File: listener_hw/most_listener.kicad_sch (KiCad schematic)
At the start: 74 parts, among them J1 1-1394640-1, J2 ANALYSER, J3 I2S, J4 VBAT_IN, M1 Tang Nano 20K, M2 ESP32-DevKitC-VIE, U1 74LVC1G34, U10 TPS2553DBVR, U11 74LVC1G123, U2 74LVC1G157, U3 74LVC1G125, U4 74LVC1G123, U5 TPS7B8133DRV, U6 LMR33630ADDA, U7 Si514, U8 LP5907MFX-3.3, U9 74LVC1G79

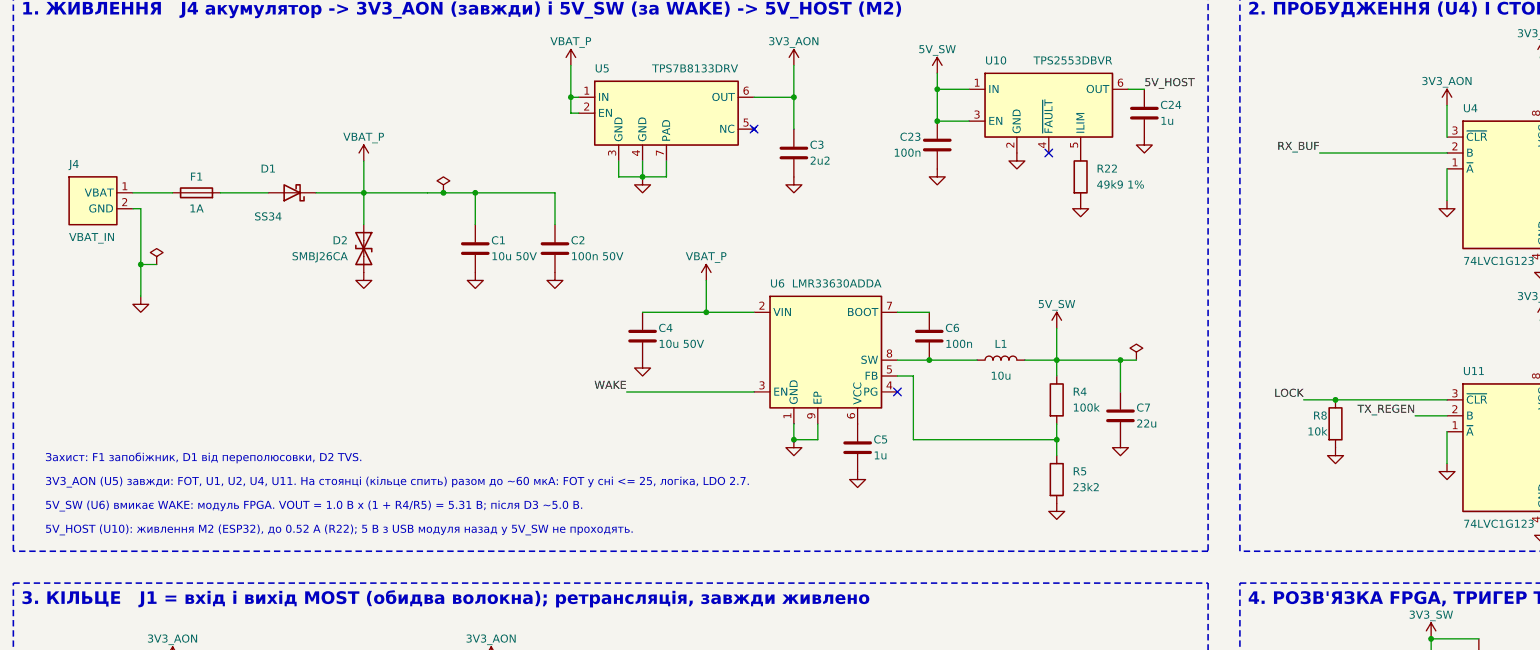
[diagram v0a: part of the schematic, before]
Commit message: Board: about 1 A for the host module's supply, not 0.52 A
U10 (TPS2553) limited 5V_HOST to 0.52 A typ (0.475-0.565 A, R22 49.9k).
Espressif asks for a 500 mA supply for the ESP32 module and its radio
draws it in peaks: a brown-out reset waiting to happen, with 1 uF behind
the switch. R22 24.9k (about 1 A; the limit scales with 1/R from the
table's 0.52 A at 49.9k), C24 10 uF. The sheet and its PDF regenerated;
ERC 0/0.

Co-Authored-By: Claude Fable 5.1 <noreply@anthropic.com>
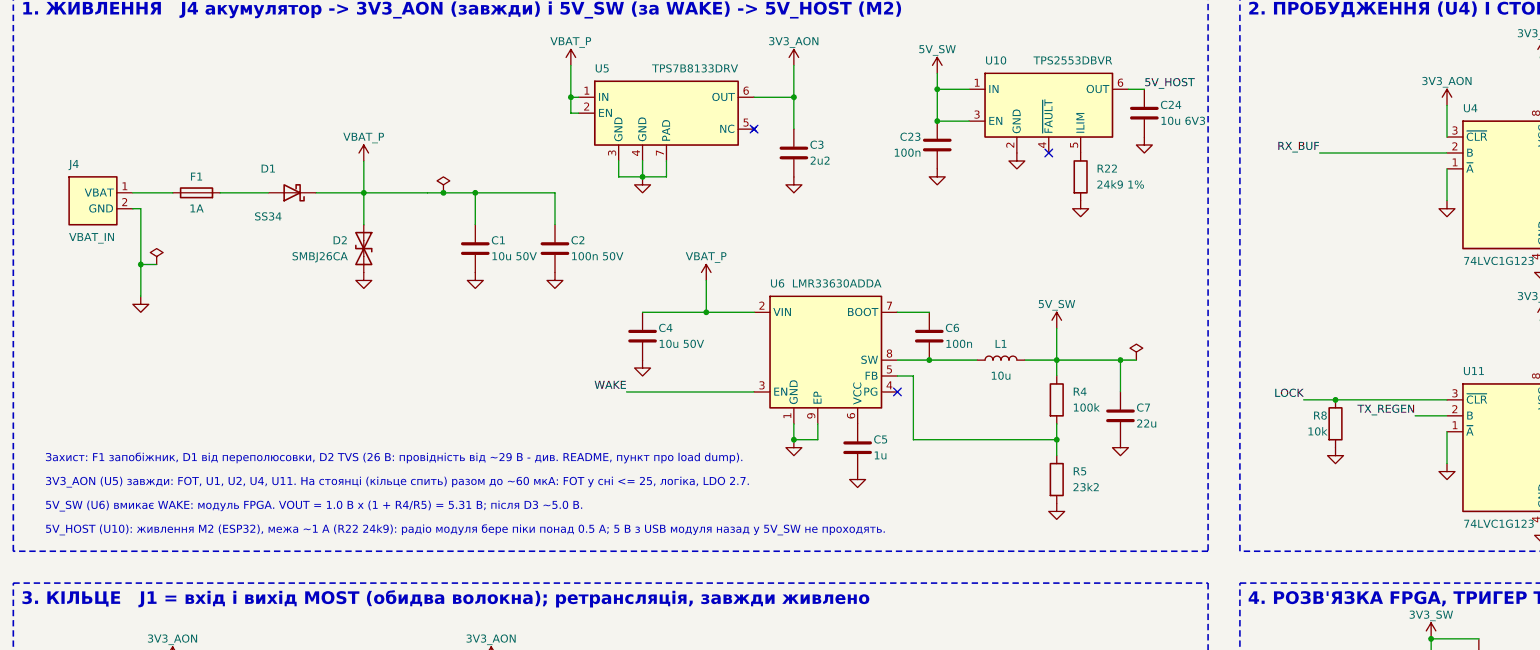
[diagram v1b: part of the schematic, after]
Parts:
- C24: value 1u -> 10u 6V3; footprint Capacitor_SMD:C_0603_1608Metric -> Capacitor_SMD:C_0805_2012Metric
- R22: value 49k9 1% -> 24k9 1%
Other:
- note added: "5V_HOST (U10): живлення M2 (ESP32), межа ~1 А (R22 24k9): радіо модуля бере піки понад 0.5 А; 5 В з USB модуля назад у 5V_SW не проходять."
- note added: "Захист: F1 запобіжник, D1 від переполюсовки, D2 TVS (26 В: провідність від ~29 В - див. README, пункт про load dump)."
- note removed: "5V_HOST (U10): живлення M2 (ESP32), до 0.52 А (R22); 5 В з USB модуля назад у 5V_SW не проходять."
- note removed: "Захист: F1 запобіжник, D1 від переполюсовки, D2 TVS."
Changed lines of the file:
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@@
   (pin "1")
   (instances (project "most_listener" (path "/1dba4ab3-cb1b-59ba-ab72-d256b8063c7a" (reference "#PWR007") (unit 1)))))
-(text "Захист: F1 запобіжник, D1 від переполюсовки, D2 TVS." (exclude_from_sim no) (at 17.78 87.63 0) (effects (font (size 1.27 1.27)) (justify left bottom)))
+(text "Захист: F1 запобіжник, D1 від переполюсовки, D2 TVS (26 В: провідність від ~29 В - див. README, пункт про load dump)." (exclude_from_sim no) (at 17.78 87.63 0) (effects (font (size 1.27 1.27)) (justify left bottom)))
 (text "3V3_AON (U5) завжди: FOT, U1, U2, U4, U11. На стоянці (кільце спить) разом до ~60 мкА: FOT у сні <= 25, логіка, LDO 2.7." (exclude_from_sim no) (at 17.78 91.44 0) (effects (font (size 1.27 1.27)) (justify left bottom)))
 (text "5V_SW (U6) вмикає WAKE: модуль FPGA. VOUT = 1.0 В x (1 + R4/R5) = 5.31 В; після D3 ~5.0 В." (exclude_from_sim no) (at 17.78 95.25 0) (effects (font (size 1.27 1.27)) (justify left bottom)))
-(text "5V_HOST (U10): живлення M2 (ESP32), до 0.52 А (R22); 5 В з USB модуля назад у 5V_SW не проходять." (exclude_from_sim no) (at 17.78 99.06 0) (effects (font (size 1.27 1.27)) (justify left bottom)))
+(text "5V_HOST (U10): живлення M2 (ESP32), межа ~1 А (R22 24k9): радіо модуля бере піки понад 0.5 А; 5 В з USB модуля назад у 5V_SW не проходять." (exclude_from_sim no) (at 17.78 99.06 0) (effects (font (size 1.27 1.27)) (justify left bottom)))
 (symbol (lib_id "most_listener:TPS7B8133DRV") (at 116.84 31.75 0) (unit 1) (exclude_from_sim no) (in_bom yes) (on_board yes) (dnp no)
   (property "Reference" "U5" (at 105.41 25.4 0) (effects (font (size 1.27 1.27)) (justify left bottom)))
@@
 (symbol (lib_id "Device:R") (at 182.88 41.91 0) (unit 1) (exclude_from_sim no) (in_bom yes) (on_board yes) (dnp no)
   (property "Reference" "R22" (at 185.42 40.64 0) (effects (font (size 1.27 1.27)) (justify left)))
-  (property "Value" "49k9 1%" (at 185.42 43.18 0) (effects (font (size 1.27 1.27)) (justify left)))
+  (property "Value" "24k9 1%" (at 185.42 43.18 0) (effects (font (size 1.27 1.27)) (justify left)))
   (property "Footprint" "Resistor_SMD:R_0603_1608Metric" (at 182.88 41.91 0) (effects (font (size 1.27 1.27)) (hide yes)))
   (property "Datasheet" "" (at 182.88 41.91 0) (effects (font (size 1.27 1.27)) (hide yes)))
@@
 (symbol (lib_id "Device:C") (at 193.04 31.75 0) (unit 1) (exclude_from_sim no) (in_bom yes) (on_board yes) (dnp no)
   (property "Reference" "C24" (at 195.58 30.48 0) (effects (font (size 1.27 1.27)) (justify left)))
-  (property "Value" "1u" (at 195.58 33.02 0) (effects (font (size 1.27 1.27)) (justify left)))
-  (property "Footprint" "Capacitor_SMD:C_0603_1608Metric" (at 193.04 31.75 0) (effects (font (size 1.27 1.27)) (hide yes)))
+  (property "Value" "10u 6V3" (at 195.58 33.02 0) (effects (font (size 1.27 1.27)) (justify left)))
+  (property "Footprint" "Capacitor_SMD:C_0805_2012Metric" (at 193.04 31.75 0) (effects (font (size 1.27 1.27)) (hide yes)))
   (property "Datasheet" "" (at 193.04 31.75 0) (effects (font (size 1.27 1.27)) (hide yes)))
   (pin "1") (pin "2")

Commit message: Board: block 9, TOSLINK in through DIR9001 and SRC4192, S/PDIF out on TOSLINK and coax
J5 (PLR135/T10) -> R25 -> U12 DIR9001 in hardware mode: PLL clock recovery
from the signal, 24-bit I2S out (FMT = HH), CKSEL = L, XTI to ground (no
crystal; the frequency calculator is not used), the loop filter of Table 6.
U13 SRC4192 with both ports slave (MODE = 000): the receiver's I2S on the
receiver's clock in (IFMT = 001), I2S 24 bit on the FPGA's BCLK/LRCK out
(OFMT = 01, OWL = 00) -> I2S_DIN2_F, pin 54. X1 24.576 MHz is the rate
estimator's reference (RCKI), asynchronous to both ports. One RC gives
both chips their reset 10 ms after 3V3_SW, when X1 already runs (the
SRC4192 has no power-on reset). U12's ERROR goes to M2 IO32 (OPT_ERR): 1 =
no lock or a parity error, so the host does not inject.

S/PDIF out: SPDIF_F (FPGA pin 31) -> R28 -> J6 (PLT133/T10W), and R26/R27
(0.5 V into 75 ohm from 75 ohm) + C29 -> J7, an RCA jack. Every pinout from
the data sheets (TI SLES198A, SBFS022C; Everlight PLR135, PLT133) or the
KiCad library (ASE oscillator, coaxial connector). The sheet is A2 now;
ERC: 0 violations; the PDF regenerated.

Co-Authored-By: Claude Fable 5.1 <noreply@anthropic.com>
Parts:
- added C27: 68n, Capacitor_SMD:C_0603_1608Metric, symbol Device:C
- added C28: 4n7, Capacitor_SMD:C_0603_1608Metric, symbol Device:C
- added C29, C30, C31, C32, C34, C36, C38, C39: 100n, Capacitor_SMD:C_0603_1608Metric, symbol Device:C
- added C33, C35, C37: 10u, Capacitor_SMD:C_0805_2012Metric, symbol Device:C
- added C40: 1u, Capacitor_SMD:C_0603_1608Metric, symbol Device:C
- added FB3: 600R, Inductor_SMD:L_0603_1608Metric, symbol Device:FerriteBead
- added J5: PLR135/T10, symbol most_listener:PLR135
- added J6: PLT133/T10W, symbol most_listener:PLT133
- added J7: RCA 75R, symbol Connector:Conn_Coaxial
- added R24: 680, Resistor_SMD:R_0603_1608Metric, symbol Device:R
- added R25: 100, Resistor_SMD:R_0603_1608Metric, symbol Device:R
- added R26: 240, Resistor_SMD:R_0603_1608Metric, symbol Device:R
- added R27: 110, Resistor_SMD:R_0603_1608Metric, symbol Device:R
- added R28, R29: 33, Resistor_SMD:R_0603_1608Metric, symbol Device:R
- added R30: 10k, Resistor_SMD:R_0603_1608Metric, symbol Device:R
- added U12: DIR9001, Package_SO:TSSOP-28_4.4x9.7mm_P0.65mm, symbol most_listener:DIR9001
- added U13: SRC4192, Package_SO:SSOP-28_5.3x10.2mm_P0.65mm, symbol most_listener:SRC4192
- added X1: 24.576MHz, Oscillator:Oscillator_SMD_Abracon_ASE-4Pin_3.2x2.5mm, symbol Oscillator:ASE-xxxMHz
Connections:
- net 3V3_SW: now also C31.1, C32.1, C33.1, C34.1, C35.1, C36.1, C37.1, C38.1, C39.1, FB3.2, J6.2 (VCC), R30.1, U12.24 (VCC), U12.25 (FMT0), U12.26 (FMT1), U12.5 (VDD), U13.10 (IFMT0), U13.19 (OFMT0), U13.22 (VDD), U13.7 (VIO), X1.1 (EN), X1.4 (Vdd)
- net GND: now also C27.2, C28.2, C30.2, C31.2, C32.2, C33.2, C34.2, C35.2, C36.2, C37.2, C38.2, C39.2, C40.2, J5.2 (GND), J6.3 (GND), J7.2 (Ext), R27.2, U12.13 (PSCK0), U12.14 (PSCK1), U12.19 (RSV), U12.23 (AGND), U12.28 (CKSEL), U12.6 (DGND), U12.8 (XTI), U13.1 (LGRP), U13.11 (IFMT1), U13.12 (IFMT2), U13.14 (MUTE), U13.16 (OWL1), U13.17 (OWL0), U13.18 (OFMT1), U13.20 (TDMI), U13.21 (DGND), U13.26 (MODE0), U13.27 (MODE1), U13.28 (MODE2), U13.8 (DGND), U13.9 (BYPAS), X1.2 (GND)
- net I2S_BCLK_F: now also U13.25 (BCKO)
- net I2S_LRCK_F: now also U13.24 (LRCKO)
- net SPDIF_F: now reaches M1.14 (31 LCD_B3)
- net SPDIF_F: now also R26.1, R28.1
- net I2S_DIN2_F: now reaches M1.28 (54 I2S_DIN)
- net I2S_DIN2_F: now also R29.2
- net OPT_ERR: now reaches M2.7 (IO32)
- net OPT_ERR: now also U12.27 (ERROR)
- new net: J6.1 (VIN), R28.2
- new net: C29.1, R26.2, R27.1
- new net: C29.2, J7.1 (In)
- new net: U13.2 (RCKI), X1.3 (OUT)
- new net: R29.1, U13.23 (SDOUT)
- new net: U12.12 (DOUT), U13.4 (SDIN)
- new net: U12.11 (BCKO), U13.5 (BCKI)
- new net: U12.10 (LRCKO), U13.6 (LRCKI)
- new net: C30.1, FB3.1, J5.3 (VCC)
- new net: C27.1, R24.1
- new net: C28.1, R24.2, U12.22 (FILT)
- new net: J5.1 (VOUT), R25.1
- new net: R25.2, U12.20 (RXIN)
- new net RST_AIN: C40.1, R30.2, U12.21 (RST), U13.13 (RST)
- no-connect marks 52 -> 63
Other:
- note added: "5V_SW (U6) вмикає WAKE: модуль FPGA, з його 3V3 (3V3_SW) - блок 9 (~0.1 А). VOUT = 1.0 В x (1 + R4/R5) = 5.31 В; після D3 ~5.0 В."
- note added: "9. ЦИФРОВЕ АУДІО J5 TOSLINK IN -> U12 DIR9001 -> U13 SRC4192 -> I2S_DIN2_F; SPDIF_F -> J6 TOSLINK OUT і J7 коаксіал"
- note added: "C31 J6; C32/C33 U12 VDD; C34/C35 U12 VCC;"
- note added: "C36/C37 U13 VDD; C38 U13 VIO; C39 X1: біля виводів."
- note added: "I2S slave: IO34/35 <- BCLK/LRCK, IO27 -> DIN; IO32 <- OPT_ERR."
- note added: "J3: I2S, BCLK 64 Fs, слоти 32 біт, 24 біт з регулюваннями ГУ; те саме S/PDIF - J6, J7 (блок 9)."
- note added: "J5 TOSLINK IN -> R25 -> U12 DIR9001: PLL відновлює такт із сигналу, вихід I2S 24 біт (FMT1 FMT0 = HH), CKSEL = L. XTI на землю: кварц не потрібен."
- note added: "OPT_ERR (U12 ERROR) -> M2 IO32: 1 = TOSLINK без сигналу або помилка парності; хост тоді не інжектує. Джерело для інжекції: команда 02, біт M[2]."
- note added: "S/PDIF OUT: SPDIF_F (FPGA 31) -> R28 -> J6 PLT133; R26/R27: 0.5 В на 75 Ом, вихідний опір 75 Ом; C29 без постійної -> J7 RCA. Той самий потік, що й на J3."
- note added: "U13 SRC4192: обидва порти slave (MODE = 000); вхід I2S 24 біт (IFMT = 001) від U12; вихід I2S 24 біт (OFMT = 01, OWL = 00) на тактах FPGA -> I2S_DIN2_F."
- note added: "X1 24.576 МГц: опорний такт оцінювача швидкості SRC4192 (RCKI), асинхронний до обох портів. RST_AIN: R30/C40 = 10 мс, коли X1 уже іде (SRC4192 без POR)."
- note added: "Кільце і Si514 - лише на виводах LCD (порожній роз'єм); S/PDIF на 31 (LCD_B3). HSPI, TF (80, 85), 54 (I2S_DIN вбудованого ЦАП): UART, MCLK, I2S, SD1, DIN2."
- note removed: "5V_SW (U6) вмикає WAKE: модуль FPGA. VOUT = 1.0 В x (1 + R4/R5) = 5.31 В; після D3 ~5.0 В."
- note removed: "I2S slave: IO34/35 <- BCLK/LRCK, IO27 -> DIN."
- note removed: "J3: I2S, BCLK 64 Fs, слоти 32 біт, 24 біт з регулюваннями ГУ."
- note removed: "Кільце і Si514 - лише на виводах LCD (порожній роз'єм). На HSPI і TF (80, 85) - лише UART, MCLK, I2S, SD1."

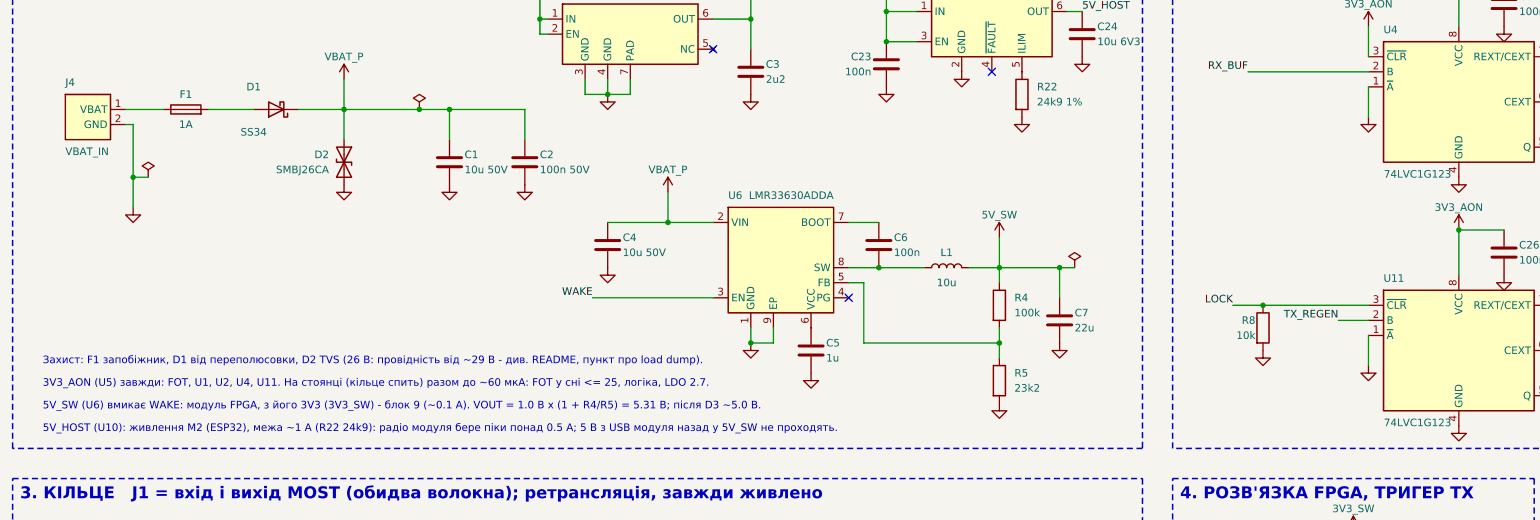
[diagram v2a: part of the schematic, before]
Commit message: Board: the battery input for ISO 16750-2 test B and ISO 7637-2 pulses - LMR38020, SMBJ36A before D1, a slow fuse
The SMBJ26CA behind the reverse diode conducted from 28.9 V: a suppressed
load dump (35 V, up to 400 ms, 0.5..4 ohm) that the buck itself survives
would have burnt it and blown F1, and a negative pulse 1 (-150 V, 10 ohm)
reached D1's 40 V reverse rating before any TVS clamped it. A TVS silent at
35 V clamps the fast pulses at 42..53 V, above the LMR33630's 38 V absolute
maximum, so the buck had to change too.

Now: U6 LMR38020F (4.2..80 V in, 85 V absolute maximum, 2 A, 400 kHz from
R31 = 64.9 k per Table 8-1, forced PWM so the frequency never falls into the
audio band; L1 15 uH and C7 47 uF per Table 9-1, CIN 4.7 uF + 100 nF at
100 V per 9.2.2.6; PG open, RT/SYNC never floats). D2 SMBJ36A,
unidirectional, between F1 and D1: silent at 35 V, clamps pulse 2a around
50 V, shunts negative pulses through its forward diode so D1 sees the
battery plus a volt. F1 2 A slow-blow: pulse 1 drives up to 15 A through the
TVS for 2 ms. C1, C2 rated 100 V for the clamped transients. Pins from TI
SNVSC40E Table 6-1 (the DDA pinout differs from the LMR33630's). Not
covered: the unsuppressed load dump (test A) - a 6.6 kW TVS's job. ERC 0
violations, PDF regenerated, README's open decision closed.

Co-Authored-By: Claude Fable 5.1 <noreply@anthropic.com>
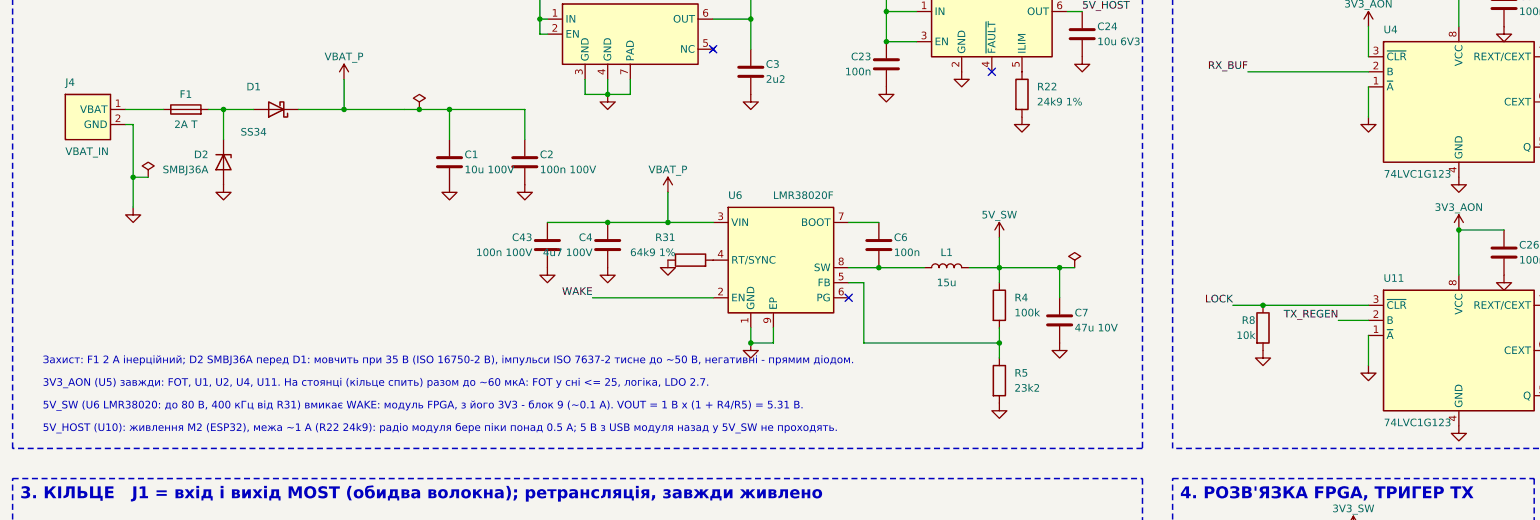
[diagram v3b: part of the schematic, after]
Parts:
- removed C5: 1u, Capacitor_SMD:C_0603_1608Metric, symbol Device:C
- added C43: 100n 100V, Capacitor_SMD:C_0603_1608Metric, symbol Device:C
- added R31: 64k9 1%, Resistor_SMD:R_0603_1608Metric, symbol Device:R
- C1: value 10u 50V -> 10u 100V
- C2: value 100n 50V -> 100n 100V
- C4: value 10u 50V -> 4u7 100V
- C7: value 22u -> 47u 10V; footprint Capacitor_SMD:C_1206_3216Metric -> Capacitor_SMD:C_1210_3225Metric
- D2: value SMBJ26CA -> SMBJ36A; symbol Device:D_TVS -> Device:D_Zener
- F1: value 1A -> 2A T
- L1: value 10u -> 15u
- U6: value LMR33630ADDA -> LMR38020F; symbol most_listener:LMR33630ADDA -> most_listener:LMR38020DDA
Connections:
- net GND: now also C43.2, R31.1
- net VBAT_P: now also U6.3 (VIN), C43.1; no longer D2.1 (A1), U6.2 (VIN)
- net WAKE: now also U6.2 (EN); no longer U6.3 (EN)
- net at U6.4 (RT/SYNC): now also R31.2
- net at D1.2 (A), F1.2: now also D2.1 (K)
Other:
- note added: "5V_SW (U6 LMR38020: до 80 В, 400 кГц від R31) вмикає WAKE: модуль FPGA, з його 3V3 - блок 9 (~0.1 А). VOUT = 1 В x (1 + R4/R5) = 5.31 В."
- note added: "Захист: F1 2 А інерційний; D2 SMBJ36A перед D1: мовчить при 35 В (ISO 16750-2 B), імпульси ISO 7637-2 тисне до ~50 В, негативні - прямим діодом."
- note removed: "5V_SW (U6) вмикає WAKE: модуль FPGA, з його 3V3 (3V3_SW) - блок 9 (~0.1 А). VOUT = 1.0 В x (1 + R4/R5) = 5.31 В; після D3 ~5.0 В."
- note removed: "Захист: F1 запобіжник, D1 від переполюсовки, D2 TVS (26 В: провідність від ~29 В - див. README, пункт про load dump)."
- moved on the sheet: D2
